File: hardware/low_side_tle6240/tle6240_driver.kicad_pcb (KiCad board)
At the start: 2 copper layers, 42.7 x 56.5 mm, 12 parts, among them K1 JUMPER3, K2 CONN_3, P1 CONN_10X2, P2 CONN_16, P3 CONN_2X2

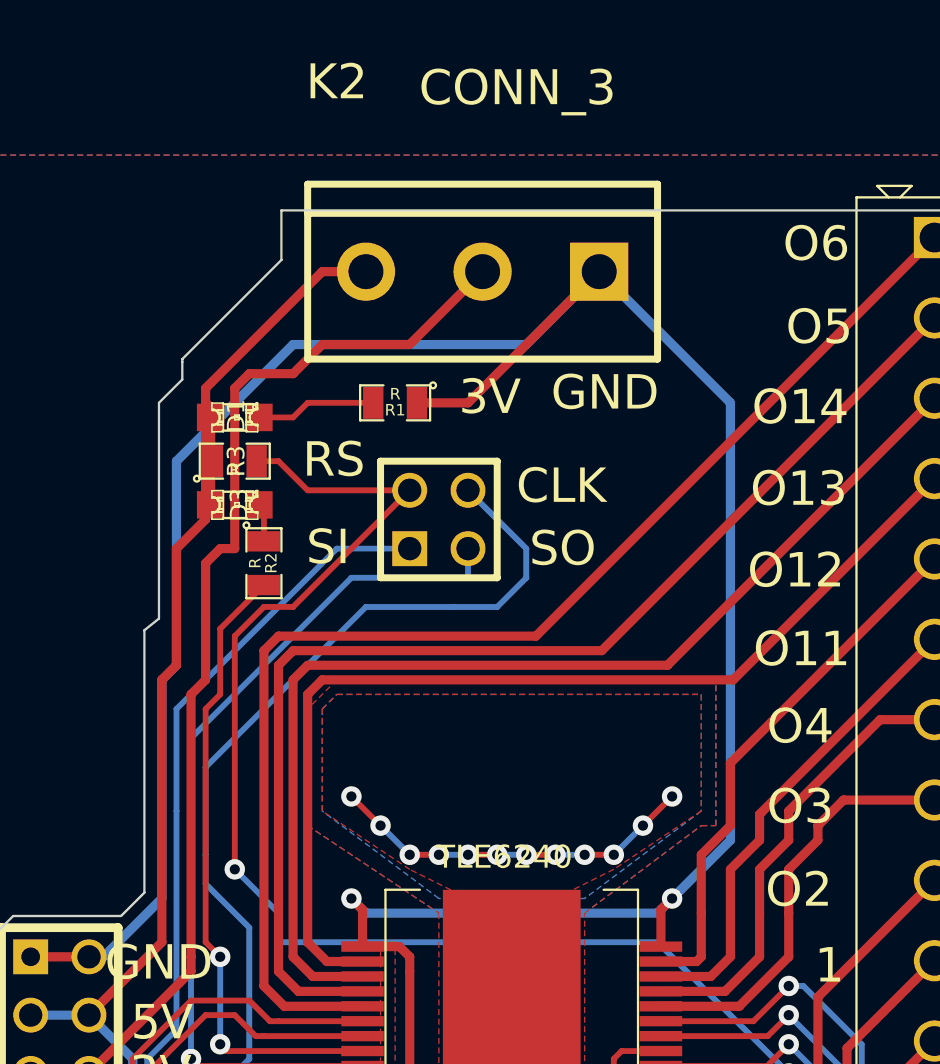
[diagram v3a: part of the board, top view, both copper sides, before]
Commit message: 
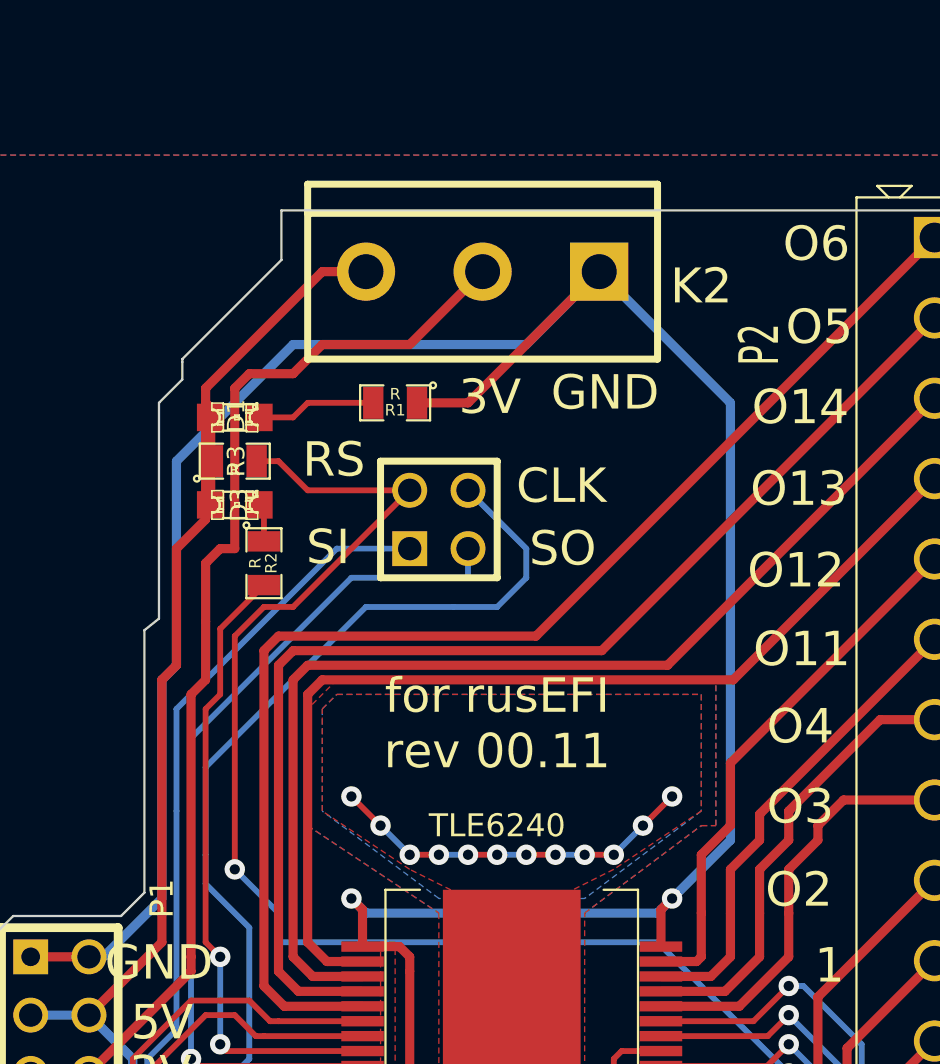
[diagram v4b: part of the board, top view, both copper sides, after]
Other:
- net class Default: clearance 0 -> 0.012
- rule trace_clearance: 0 -> 0.012
- board text added: "for rusEFI rev 00.11"
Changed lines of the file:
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@@
     (links 53)
     (no_connects 0)
-    (area 120.639999 87.8316 223.928 190.510001)
+    (area 120.639999 88.0856 223.928 190.510001)
     (thickness 1.6)
-    (drawings 66)
+    (drawings 67)
     (tracks 403)
     (zones 0)
@@
     (user_trace_width 3.6068)
     (user_trace_width 9.3472)
-    (trace_clearance 0)
+    (trace_clearance 0.012)
     (zone_clearance 0.4)
     (zone_45_only no)
@@
     (pad_to_mask_clearance 0)
     (aux_axis_origin 0 0)
-    (visible_elements 7FFFFFFF)
+    (visible_elements 7FFFFF3F)
     (pcbplotparams
       (layerselection 284983297)
@@
   (net 36 N-0000023)
   (net_class Default "This is the default net class."
-    (clearance 0)
+    (clearance 0.012)
     (trace_width 0.254)
     (via_dia 0.889)
@@
     (descr "Double rangee de contacts 2 x 10 pins")
     (tags CONN)
-    (fp_text reference P1 (at 0 -3.81 270) (layer F.SilkS) hide
+    (fp_text reference P1 (at -13.97 -4.445 270) (layer F.SilkS)
       (effects (font (size 1.016 1.016) (thickness 0.254)))
     )
@@
       (effects (font (size 1 1) (thickness 0.15)))
     )
-    (fp_text value TLE6240 (at 0.325 9.425 180) (layer F.SilkS)
+    (fp_text value TLE6240 (at 0.635 10.795 180) (layer F.SilkS)
       (effects (font (size 1 1) (thickness 0.15)))
     )
@@
     (descr "Bornier d'alimentation 3 pins")
     (tags DEV)
-    (fp_text reference K2 (at 6.35 8.255 180) (layer F.SilkS)
+    (fp_text reference K2 (at -9.525 -0.635 180) (layer F.SilkS)
       (effects (font (size 1.524 1.524) (thickness 0.3048)))
     )
-    (fp_text value CONN_3 (at -1.524 8.001 180) (layer F.SilkS)
+    (fp_text value CONN_3 (at -1.524 8.001 180) (layer F.SilkS) hide
       (effects (font (size 1.524 1.524) (thickness 0.3048)))
     )
@@
     (at 217.17 121.92 270)
     (descr "14 PIN 3.5MM")
-    (fp_text reference P2 (at -28.5115 -5.3975 270) (layer F.SilkS) hide
+    (fp_text reference P2 (at -21.59 7.62 270) (layer F.SilkS)
       (effects (font (size 1.72974 1.08712) (thickness 0.27178)))
     )
@@
     )
   )
+  (gr_text "for rusEFI\nrev 00.11" (at 198.12 116.84) (layer F.SilkS)
+    (effects (font (size 1.5 1.5) (thickness 0.3)))
+  )
   (gr_text GND (at 183.388 127.254) (layer F.SilkS)
